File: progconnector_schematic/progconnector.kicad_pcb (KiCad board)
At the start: 2 copper layers, 28.5 x 14 mm, 10 parts, among them J1 Screw_Terminal_1x01, J10 Screw_Terminal_1x01, J2 Screw_Terminal_1x01, J3 Screw_Terminal_1x01, J4 Screw_Terminal_1x01, J5 Screw_Terminal_1x01, J6 Screw_Terminal_1x01, J7 Screw_Terminal_1x01, J8 Screw_Terminal_1x01, J9 Screw_Terminal_1x01

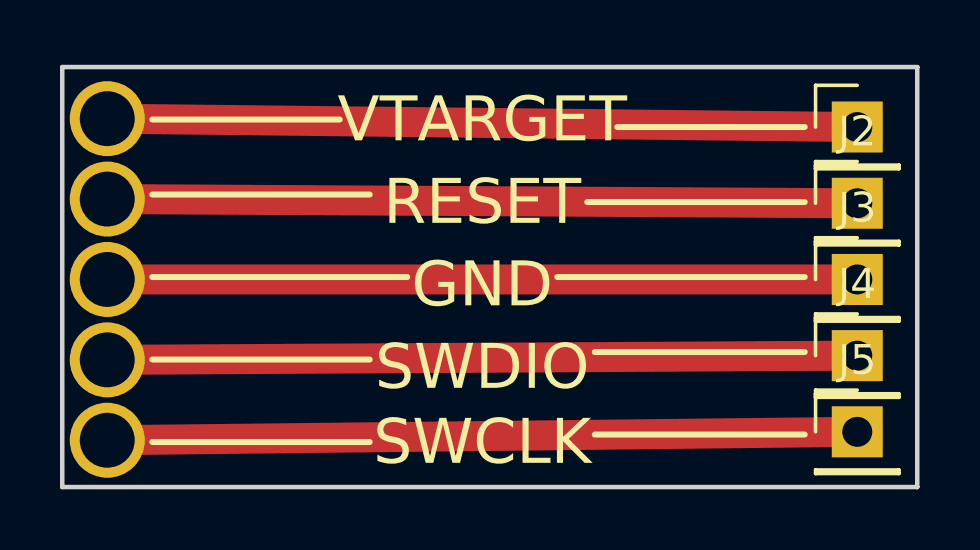
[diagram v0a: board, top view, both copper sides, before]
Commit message: Work on programming connector board.
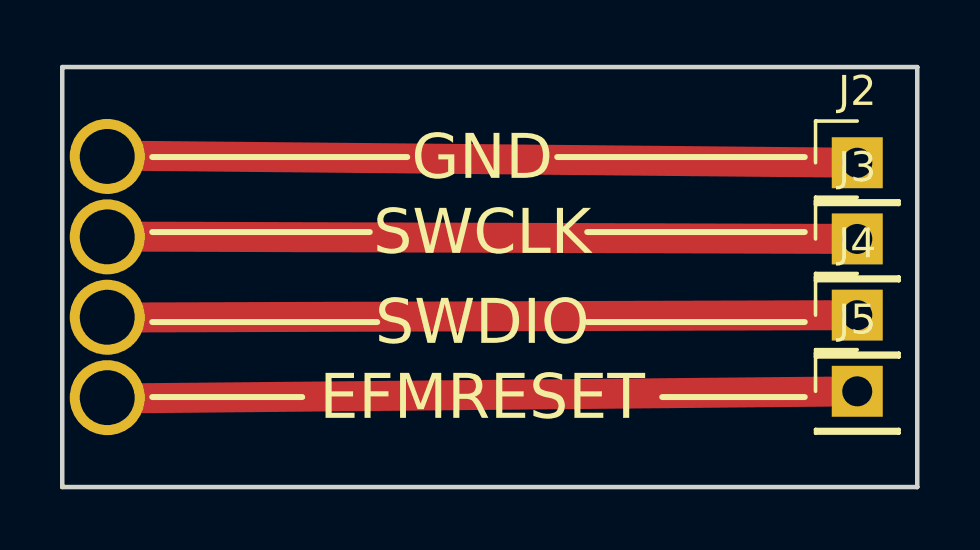
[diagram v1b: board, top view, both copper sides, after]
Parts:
- removed J1: Screw_Terminal_1x01, Pin_Headers:Pin_Header_Straight_1x01_Pitch2.54mm
- removed J6: Screw_Terminal_1x01, newlightmeter:POGOHOLDER
- moved J2 1.35 mm to (100.0, 51.2)
- moved J3 1.35 mm to (100.0, 53.7)
- moved J4 1.35 mm to (100.0, 56.3)
- moved J5 1.35 mm to (100.0, 58.8)
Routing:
- net Net-(J1-Pad1): track 25.0 -> 0.00 mm
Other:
- board text added: "EFMRESET"
- board text removed: "RESET"
- board text removed: "VTARGET"
